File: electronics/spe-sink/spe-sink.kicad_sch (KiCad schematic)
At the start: 18 parts, among them Q1 2N7002P, U1 ATL431LIB, U2 MCP65R41T, U3 AP7375-33

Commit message: Continue work on PD function board schematic
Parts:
- added C10, C12, C14, C6, C8: 100n_X7R_1005M, Applidyne_Capacitor:CAPC1005X60N, symbol appli_capacitor:100n_X7R_1005M
- added C11, C13, C9: 10n_X7R_1005M, Applidyne_Capacitor:CAPC1005X60N, symbol appli_capacitor:10n_X7R_1005M
- added C15: 1u_X5R_1005M, Applidyne_Capacitor:CAPC1005X60N, symbol appli_capacitor:1u_X5R_1005M
- added C16, C17: 22p_X7R_1608M, CAPC1608*, symbol appli_capacitor:22p_X7R_1608M
- added C18, C19: 10u_X7R_2012M, CAPC2012*, symbol appli_capacitor:10u_X7R_2012M
- added C20, C21: 100n_X7R_1608M, CAPC1608*, symbol appli_capacitor:100n_X7R_1608M
- added C5: 4n7_X7R_1608M, CAPC1608*, symbol appli_capacitor:4n7_X7R_1608M
- added C7: 470n_X5R_1005M, CAPC1005X60*, symbol appli_capacitor:470n_X5R_1005M
- added IC1: AT24C02C-SSHM, Applidyne_SOIC:SOIC127P600X330-8L2N, symbol appli_memory:AT24C02C-SSHM
- added P1: CONN_01X03, Applidyne_Connector_Wurth:61300311121, symbol appli_connector_wurth:CONN_01X03
- added R10: 1K5_1005M, Applidyne_Resistor:RESC1005X40N, symbol appli_resistor:1K5_1005M
- added R11: 10K0_1608M, Applidyne_Resistor:RESC1608X50N, symbol appli_resistor:10K0_1608M
- added R12: 100K_1608M, Applidyne_Resistor:RESC1608X50N, symbol appli_resistor:100K_1608M
- added SL1: SOLDER-LINK-3, SJ1608-3*, symbol appli_link:SOLDER-LINK-3
- added SL2: SOLDER-LINK-2-TINY, Applidyne_Link:SJ1005-2N, symbol appli_link:SOLDER-LINK-2-TINY
- added TEST2: CLIP_HOOK_BLUE, Applidyne_Test:KEYSTONE_5117, symbol appli_test_points:CLIP_HOOK_BLUE
- added U4: ADIN1110, Applidyne_QFN:QFN50P600X600X100-40T350X350N, symbol appli_special:ADIN1110
- added U5: AP2112K-3.3, Applidyne_SOT:SOT95P280X145-5L30N, symbol appli_regulator:AP2112K-3.3
- added U6: INA180A3, Applidyne_SOT:SOT23-8P65_280X145L45X30N, symbol appli_analog_devices:INA180A3
- added X1: RH100-25.000-13-F-0715, Applidyne_Crystal:OSCCC320X250X60L90X100N, symbol appli_crystal:RH100-25.000-13-F-0715
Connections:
- net GND: now also C10.2, C11.2, C12.2, C13.2, C14.2, C15.2, C16.2, C17.2, C18.2, C19.2, C20.2, C21.2, C5.2, C6.2, C7.2, C8.2, C9.2, IC1.4 (GND), SL1.3, SL2.2, U4.EP (EP(GND)), U5.2 (GND), U6.2 (GND), X1.2, X1.4
- new net: IC1.7 (WP), R12.2, SL2.1
- new net: C14.1, U4.19 (CEXT_2)
- new net: C15.1, U4.20 (CEXT_3)
- new net: C6.1, C7.1, U4.23 (DLDO_1P1), U4.24 (DVDD_1P1)
- new net: R10.2, U4.26 (TEST1)
- new net: C16.1, U4.8 (XTAL_I/CLK_IN), X1.3
- new net: C17.1, U4.9 (XTAL_O), X1.1
- new net: C18.1, R11.1, U5.1 (VIN)
- new net: R11.2, U5.3 (EN)
- new net: TEST2.1 (PAD), U6.1 (Vout)
- new net: P1.1 (P1), SL1.2
- new net: C5.1, SL1.1
- new net +3.3V: C10.1, C11.1, C12.1, C13.1, C19.1, C20.1, C21.1, C8.1, C9.1, IC1.8 (VCC), R10.1, R12.1, U4.16 (AVDD_H), U4.17 (AVDD_H), U4.22 (AVDD_L), U4.35 (VDDIO), U5.5 (VOUT), U6.5 (VCC)
- no-connect marks 0 -> 2
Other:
- note added: "AVDDH Pin 16"
- note added: "AVDDIO Pin 35"
- note added: "AVDDL Pin 22"
- note added: "Consider ideal diode to prevent LDO being backfed from the output capacitor when line goes low?"
- note added: "DS asks for 0.68uF"
- note added: "Intentionally left open-circuit"
- note added: "Internal bandgap bypass caps"
- note added: "TODO: Connect to MicroMod analog IO"
- note added: "TODO: Consider allowing PWR_EN via MicroMod pin?"
- note added: "TODO: Filter circuit"
- note added: "TODO: Screw terminal block?"
- note added: "TODO: Size shunt for 1A peak loads?"
- note added: "Write protected when high"
- note removed: "ADIN1110 SPE PHY+MAC"
- note removed: "Screw terminal"
- moved on the sheet: C1, C2, C3, C4, Q1, R1, R2, R3, R4, R5, R6, R7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

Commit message: Add MAC+PHY, other parts to PD function board sch
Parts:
- removed C1, C20, C21: 100n_X7R_1608M, CAPC1608*, symbol appli_capacitor:100n_X7R_1608M
- removed C10, C12, C14, C6, C8: 100n_X7R_1005M, Applidyne_Capacitor:CAPC1005X60N, symbol appli_capacitor:100n_X7R_1005M
- removed C11, C13, C9: 10n_X7R_1005M, Applidyne_Capacitor:CAPC1005X60N, symbol appli_capacitor:10n_X7R_1005M
- removed C15: 1u_X5R_1005M, Applidyne_Capacitor:CAPC1005X60N, symbol appli_capacitor:1u_X5R_1005M
- removed C16, C17: 22p_X7R_1608M, CAPC1608*, symbol appli_capacitor:22p_X7R_1608M
- removed C18, C19, C4: 10u_X7R_2012M, CAPC2012*, symbol appli_capacitor:10u_X7R_2012M
- removed C2: 330p_X7R_1608M, CAPC1608*, symbol appli_capacitor:330p_X7R_1608M
- removed C3: 56n_X7R_1608M, CAPC1608*, symbol appli_capacitor:56n_X7R_1608M
- removed C7: 470n_X5R_1005M, CAPC1005X60*, symbol appli_capacitor:470n_X5R_1005M
- removed IC1: AT24C02C-SSHM, Applidyne_SOIC:SOIC127P600X330-8L2N, symbol appli_memory:AT24C02C-SSHM
- removed Q1: 2N7002P, SOT23, symbol appli_transistor:2N7002P
- removed R1, R12: 100K_1608M, Applidyne_Resistor:RESC1608X50N, symbol appli_resistor:100K_1608M
- removed R10: 1K5_1005M, Applidyne_Resistor:RESC1005X40N, symbol appli_resistor:1K5_1005M
- removed R11, R5: 10K0_1608M, Applidyne_Resistor:RESC1608X50N, symbol appli_resistor:10K0_1608M
- removed R2: 9K09_1608M, Applidyne_Resistor:RESC1608X50N, symbol appli_resistor:9K09_1608M
- removed R3: 20K0_1608M, Applidyne_Resistor:RESC1608X50N, symbol appli_resistor:20K0_1608M
- removed R4: 22R_1608M, Applidyne_Resistor:RESC1608X50N, symbol appli_resistor:22R_1608M
- removed R6, R8: 470K_1608M, Applidyne_Resistor:RESC1608X50N, symbol appli_resistor:470K_1608M
- removed R7: 1M_1608M, Applidyne_Resistor:RESC1608X50N, symbol appli_resistor:1M_1608M
- removed R9: 0R_1005M, Applidyne_Resistor:RESC1005X40N, symbol appli_resistor:0R_1005M
- removed SL2: SOLDER-LINK-2-TINY, Applidyne_Link:SJ1005-2N, symbol appli_link:SOLDER-LINK-2-TINY
- removed TEST1: CLIP_HOOK_ORANGE, Applidyne_Test:KEYSTONE_5003, symbol appli_test_points:CLIP_HOOK_ORANGE
- removed TEST2: CLIP_HOOK_BLUE, Applidyne_Test:KEYSTONE_5117, symbol appli_test_points:CLIP_HOOK_BLUE
- removed U1: ATL431LIB, Applidyne_SOT:SOT95P240X110-3L16N, symbol appli_device:ATL431LI_SOT23
- removed U2: MCP65R41T, Applidyne_SOT:SOT95P240X110-6L16N, symbol appli_linear:MCP65R41T
- removed U3: AP7375-33, Applidyne_SOT:SOT95P240X110-3L16N, symbol appli_regulator:AP7375-33
- removed U4: ADIN1110, Applidyne_QFN:QFN50P600X600X100-40T350X350N, symbol appli_special:ADIN1110
- removed U5: AP2112K-3.3, Applidyne_SOT:SOT95P280X145-5L30N, symbol appli_regulator:AP2112K-3.3
- removed U6: INA180A3, Applidyne_SOT:SOT23-8P65_280X145L45X30N, symbol appli_analog_devices:INA180A3
- removed X1: RH100-25.000-13-F-0715, Applidyne_Crystal:OSCCC320X250X60L90X100N, symbol appli_crystal:RH100-25.000-13-F-0715
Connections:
- no-connect marks 2 -> 0
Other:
- added sheet Ethernet MAC+PHY (ethernet.kicad_sch)
- added sheet MicroMod Function Board (micromod.kicad_sch)
- added sheet PoDL Device Handling (podl-pd.kicad_sch.kicad_sch)
- added sheet Power Regulation (power.kicad_sch)
- note added: "Filter/Coupling Network"
- note removed: "AVDDH Pin 16"
- note removed: "AVDDIO Pin 35"
- note removed: "AVDDL Pin 22"
- note removed: "Alternative: 4.54k 10.0k"
- note removed: "Bulk Regulator"
- note removed: "CYA/TESTPOINT"
- note removed: "Consider ideal diode to prevent LDO being backfed from the output capacitor when line goes low?"
- note removed: "DS asks for 0.68uF"
- note removed: "Intentionally left open-circuit"
- note removed: "Internal bandgap bypass caps"
- note removed: "Optional SCCP circuit would go here!"
- note removed: "PoDL DETECTION CIRCUIT"
- note removed: "TODO: Connect to MicroMod analog IO"
- note removed: "TODO: Consider allowing PWR_EN via MicroMod pin?"
- note removed: "TODO: Filter circuit"
- note removed: "TODO: Size shunt for 1A peak loads?"
- note removed: "The PSE tests the PD with a 9-mA to 16-mA constant current pulse. Need to provide the signature voltage from 4.05 V to 4.55 V. Then PSE will enable full power output."
- note removed: "Use precision resistors"
- note removed: "V_{DIV} = (V_{CC}*R_{A})/(R_{A}+R_{B}) = (4.05V*1M)/(1M+470K) = 4.05V"
- note removed: "V_{HYSTERESIS} = (V_{CC}*R_{A})/(R_{A}+R_{B}) = (3.3V*10K)/(10K+470K) = ~0.067V"
- note removed: "V_{REF}=2500mV I_{REF}=0.4uA V_{OUT} = (1+R_{A}/R_{B})*V_{REF}-I_{REF}*R_{A} = (1+9K09/20K)*2.5V (I_{REF} basically 0) = 3.656V"
- note removed: "Write protected when high"

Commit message: Building out PDoE filter/isolation, etc
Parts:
- added D4: CD-HD2006L, Applidyne_Device:CD-HD2x(L), symbol appli_device:CD-HD2006L
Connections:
- net GND: now also D4.4 (-)
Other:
- sheet Ethernet MAC+PHY ports: added none; removed RXN, RXP, TXN, TXP
- note removed: "Rectifier"
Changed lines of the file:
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@@
+    (stroke (width 0) (type default))
+  )
+  (wire (pts (xy 86.36 123.19) (xy 104.14 123.19))
     (stroke (width 0) (type default))
   )
@@
     (stroke (width 0) (type default))
   )
+  (wire (pts (xy 86.36 101.6) (xy 86.36 123.19))
+    (stroke (width 0) (type default))
+  )
   (wire (pts (xy 165.1 50.8) (xy 203.2 50.8))
     (stroke (width 0) (type default))
   )
+  (wire (pts (xy 92.71 101.6) (xy 92.71 102.87))
+    (stroke (width 0) (type default))
+  )
   (wire (pts (xy 35.56 60.96) (xy 35.56 64.77))
     (stroke (width 0) (type default))
@@
     (stroke (width 0) (type default))
   )
+  (wire (pts (xy 96.52 113.03) (xy 93.98 113.03))
+    (stroke (width 0) (type default))
+  )
   (wire (pts (xy 43.18 48.26) (xy 54.61 48.26))
     (stroke (width 0) (type default))
   )
+  (wire (pts (xy 104.14 120.65) (xy 104.14 123.19))
+    (stroke (width 0) (type default))
+  )
   (wire (pts (xy 43.18 50.8) (xy 54.61 50.8))
     (stroke (width 0) (type default))
   )
+  (wire (pts (xy 104.14 105.41) (xy 104.14 102.87))
+    (stroke (width 0) (type default))
+  )
+  (wire (pts (xy 111.76 113.03) (xy 119.38 113.03))
+    (stroke (width 0) (type default))
+  )
   (wire (pts (xy 35.56 69.85) (xy 35.56 72.39))
     (stroke (width 0) (type default))
   )
+  (wire (pts (xy 92.71 102.87) (xy 104.14 102.87))
+    (stroke (width 0) (type default))
+  )
   (wire (pts (xy 50.8 60.96) (xy 54.61 60.96))
     (stroke (width 0) (type default))
   )
+  (wire (pts (xy 93.98 113.03) (xy 93.98 114.3))
+    (stroke (width 0) (type default))
+  )
   (wire (pts (xy 40.64 60.96) (xy 35.56 60.96))
     (stroke (width 0) (type default))
-  )
-  (text "Rectifier" (at 92.71 110.49 0)
-    (effects (font (size 1.27 1.27)) (justify left bottom))
   )
   (text "Filter/Coupling Network" (at 82.55 77.47 0)
@@
   (text "Spec asks for <400nF input capacitance" (at 38.1 31.75 0)
     (effects (font (size 1.27 1.27)) (justify left bottom))
+  )
+  (symbol (lib_id "appli_device:CD-HD2006L") (at 104.14 113.03 0) (unit 1)
+    (in_bom yes) (on_board yes) (dnp no)
+    (property "Reference" "D4" (at 109.22 102.87 0)
+      (effects (font (size 1.27 1.27)))
+    )
+    (property "Value" "CD-HD2006L" (at 114.3 105.41 0)
+      (effects (font (size 1.27 1.27)))
+    )
+    (property "Footprint" "Applidyne_Device:CD-HD2x(L)" (at 110.236 118.999 0)
+      (effects (font (size 0.508 0.508)) (justify left bottom) hide)
+    )
+    (property "Datasheet" "https://www.bourns.com/docs/Product-Datasheets/cd-hd2xl.pdf" (at 110.236 119.634 0)
+      (effects (font (size 0.508 0.508)) (justify left bottom) hide)
+    )
+    (property "manf" "Bourns Inc" (at 110.236 120.904 0)
+      (effects (font (size 0.508 0.508)) (justify left bottom) hide)
+    )
+    (property "manf#" "CD-HD2006L" (at 110.236 121.539 0)
+      (effects (font (size 0.508 0.508)) (justify left bottom) hide)
+    )
+    (property "Supplier" "Digikey" (at 110.236 122.174 0)
+      (effects (font (size 0.508 0.508)) (justify left bottom) hide)
+    )
+    (property "Supplier Part No" "118-CD-HD2006LCT-ND" (at 110.236 122.809 0)
+      (effects (font (size 0.508 0.508)) (justify left bottom) hide)
+    )
+    (property "Supplier URL" "https://www.digikey.com.au/en/products/detail/bourns-inc/CD-HD2006L/6571504" (at 110.236 123.444 0)
+      (effects (font (size 0.508 0.508)) (justify left bottom) hide)
+    )
+    (property "Supplier Price" "1.10" (at 110.236 124.079 0)
+      (effects (font (size 0.508 0.508)) (justify left bottom) hide)
+    )
+    (property "Supplier Price Break" "10" (at 110.236 124.714 0)
+      (effects (font (size 0.508 0.508)) (justify left bottom) hide)
+    )
+    (pin "1")
+    (pin "2")
+    (pin "3")
+    (pin "4")
+    (instances
+      (project "spe-sink"
+        (path "/f0a501c7-1ad1-4c59-9255-3d6aa4545d8b"
+          (reference "D4") (unit 1)
+        )
+      )
+    )
   )
   (symbol (lib_id "appli_connector_wurth:CONN_01X03") (at 38.1 50.8 180) (unit 1)
@@
         (path "/f0a501c7-1ad1-4c59-9255-3d6aa4545d8b"
           (reference "#PWR09") (unit 1)
+        )
+      )
+    )
+  )
+  (symbol (lib_id "appli_power:GND") (at 93.98 114.3 0) (unit 1)
+    (in_bom yes) (on_board yes) (dnp no) (fields_autoplaced)
+    (property "Reference" "#PWR049" (at 93.98 120.65 0)
+      (effects (font (size 1.27 1.27)) hide)
+    )
+    (property "Value" "GND" (at 93.98 119.38 0)
+      (effects (font (size 1.27 1.27)))
+    )
+    (property "Footprint" "" (at 93.98 114.3 0)
+      (effects (font (size 1.27 1.27)) hide)
+    )
+    (property "Datasheet" "" (at 93.98 114.3 0)
+      (effects (font (size 1.27 1.27)) hide)
+    )
+    (pin "1")
+    (instances
+      (project "spe-sink"
+        (path "/f0a501c7-1ad1-4c59-9255-3d6aa4545d8b"
+          (reference "#PWR049") (unit 1)
         )
       )
@@
       (effects (font (size 1.27 1.27)) (justify left top))
     )
-    (pin "TXN" input (at 127 43.18 180)
-      (effects (font (size 1.27 1.27)) (justify left))
-    )
-    (pin "TXP" input (at 127 45.72 180)
-      (effects (font (size 1.27 1.27)) (justify left))
-    )
-    (pin "RXP" input (at 127 48.26 180)
-      (effects (font (size 1.27 1.27)) (justify left))
-    )
     (pin "{SPI}" bidirectional (at 165.1 43.18 0)
       (effects (font (size 1.27 1.27)) (justify right))
@@
       (effects (font (size 1.27 1.27)) (justify right))
     )
-    (pin "RXN" input (at 127 50.8 180)
-      (effects (font (size 1.27 1.27)) (justify left))
-    )
-    (instances
+    (instances

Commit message: PD function board schematic progress
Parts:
- added C22 (x2): 220n_X7R_1005M, Applidyne_Capacitor:CAPC1005X60N, symbol appli_capacitor:220n_X7R_1005M
- added C23: 100n_X7R_1608M, Applidyne_Capacitor:CAPC1608X90N, symbol appli_capacitor:100n_X7R_1608M
- added C25, C26, C27: 470n_X7R_2012M_100V, Applidyne_Capacitor:CAPC2012X110N, symbol appli_capacitor:470n_X7R_2012M_100V
- added C29: 1n_X7R_3216M_2kV, Applidyne_Capacitor:CAPC3216X135N, symbol appli_capacitor:1n_X7R_3216M_2kV
- added L1: WE-STST_74930000, Applidyne_Inductor:WE-STST, symbol appli_inductor:WE-STST_74930000
- added L2: COUPLED_47uH_1500mA_340mOhm, Applidyne_Inductor:WE-MCRI-1040, symbol appli_inductor:COUPLED_47uH_1500mA_340mOhm
- added L3: COMM_MODE_1000uH_800mA_0.3R, Applidyne_Inductor:WE-SL2, symbol appli_inductor:COMM_MODE_1000uH_800mA_0.2R
- added R26: 100R_1608M, Applidyne_Resistor:RESC1608X50N, symbol appli_resistor:100R_1608M
- C5: footprint CAPC1608* -> Applidyne_Capacitor:CAPC1608X90N
- SL1: footprint SJ1608-3* -> Applidyne_Link:SJ1608-3N
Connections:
- net GND: now also C23.2, C29.2
- net PoDL Device Handling/PoDL+: now reaches D4.1 (+)
- net at D4.2 (∿): now also L2.4
- net at D4.3 (∿): now also L2.1
- net at P1.2 (P2): now also L3.2
- net at P1.3 (P3): now also L3.1
- new net: C27.1, L2.2, L3.3
- new net: C26.1, L2.3, L3.4
- new net: C27.2, L1.7
- new net: C22.1, L1.1
- new net: C22.1, L1.2
- new net: C25.2, L1.3, R26.1
- new net: C25.1, L1.4
- new net: C23.1, L1.5
- new net: C26.2, L1.6
- new net: C29.1, R26.2
- new net Ethernet MAC+PHY/DATA+: C22.2
- new net Ethernet MAC+PHY/DATA-: C22.2
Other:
- sheet Ethernet MAC+PHY ports: added DATA+, DATA-; removed none
- sheet PoDL Device Handling ports: added PoDL+; removed none
- sheet Power Regulation ports: added PoDL+; removed none
- note added: "BRIDGE/LOAD 0R IF TRANSFORMER CENTER TAP CAPACITOR USED"
- note added: "Common Mode Choke"
- note added: "Differential Mode Inductor"
- note added: "ESD Protection"
- note added: "Isolation Transformer"
- note added: "Rectification"
- note added: "SPE UTP"
- note removed: "Filter/Coupling Network"
- note removed: "Input filter"
- note removed: "Spec asks for <400nF input capacitance"
- note removed: "TODO: Screw terminal block?"
- moved on the sheet: C5, D4, P1, SL1

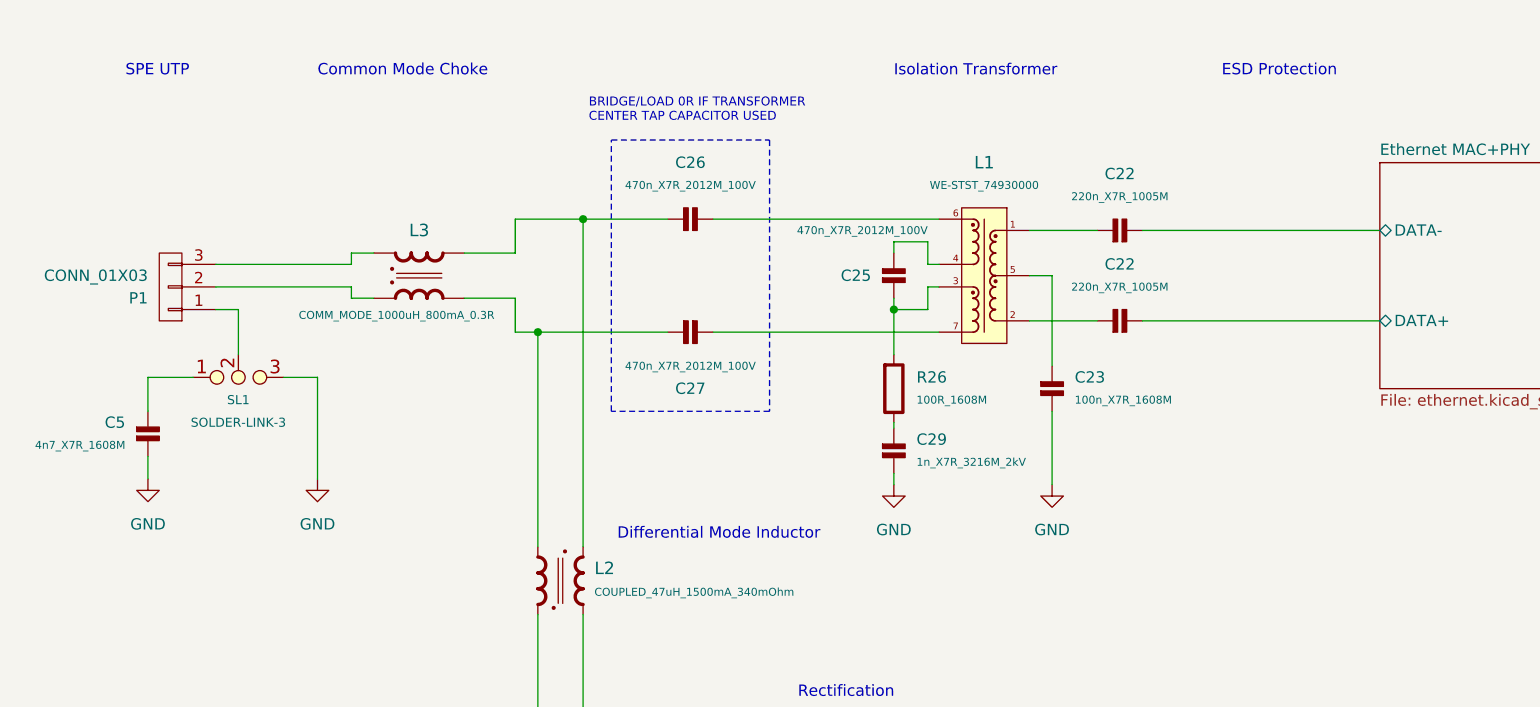
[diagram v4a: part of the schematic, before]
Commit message: PD function board bulk regulator, cleanup, part placement
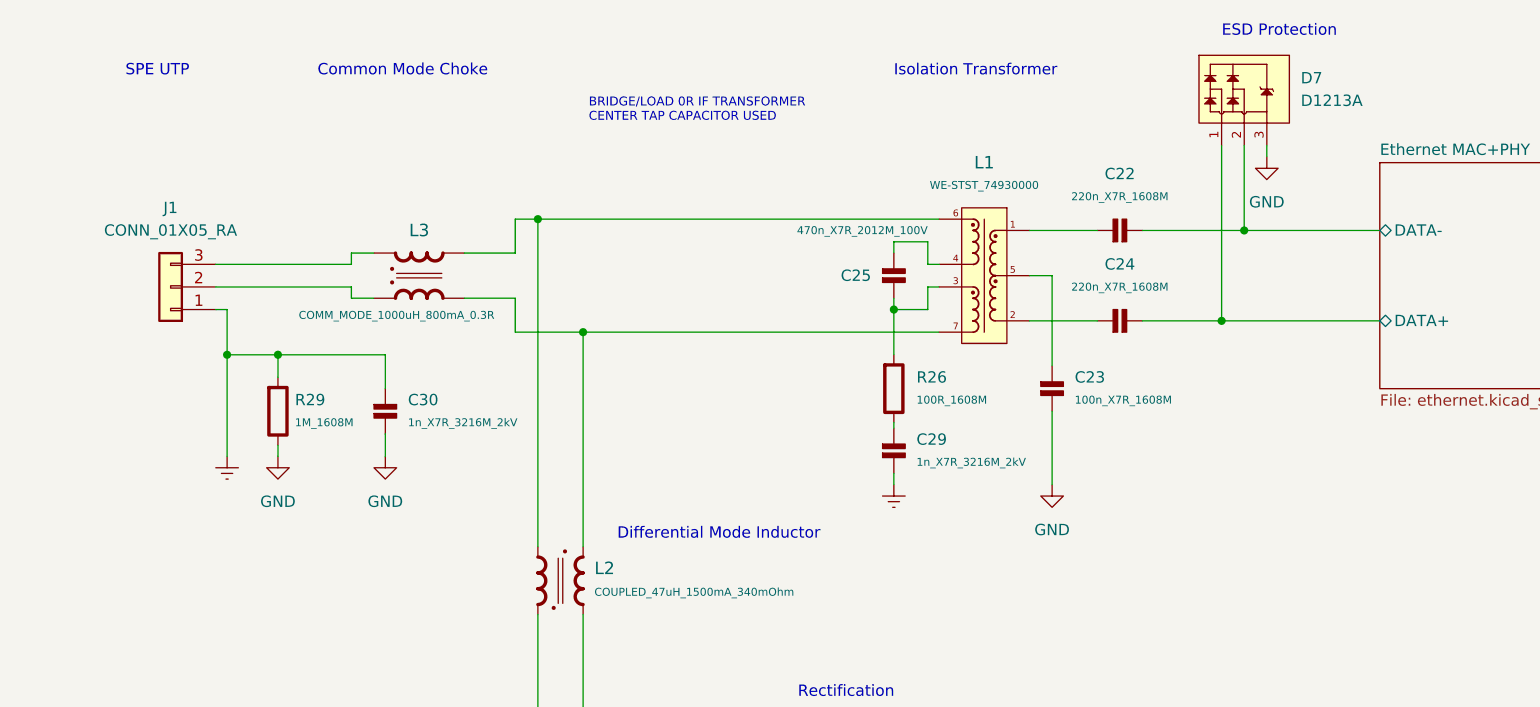
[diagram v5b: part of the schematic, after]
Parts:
- removed C22 (x2): 220n_X7R_1005M, Applidyne_Capacitor:CAPC1005X60N, symbol appli_capacitor:220n_X7R_1005M
- removed C26, C27: 470n_X7R_2012M_100V, Applidyne_Capacitor:CAPC2012X110N, symbol appli_capacitor:470n_X7R_2012M_100V
- removed C5: 4n7_X7R_1608M, Applidyne_Capacitor:CAPC1608X90N, symbol appli_capacitor:4n7_X7R_1608M
- removed P1: CONN_01X03, Applidyne_Connector_Wurth:61300311121, symbol appli_connector_wurth:CONN_01X03
- removed SL1: SOLDER-LINK-3, Applidyne_Link:SJ1608-3N, symbol appli_link:SOLDER-LINK-3
- added C22, C24: 220n_X7R_1608M, Applidyne_Capacitor:CAPC1608X90N, symbol appli_capacitor:220n_X7R_1608M
- added C30: 1n_X7R_3216M_2kV, Applidyne_Capacitor:CAPC3216X135N, symbol appli_capacitor:1n_X7R_3216M_2kV
- added D7: D1213A, Applidyne_SOT:SOT95P240X110-3L16N, symbol appli_device:D1213A
- added J1: CONN_01X05_RA, Applidyne_Connector:CUI_TBL009-254-03, symbol appli_connector:CONN_01X03_RA
- added R29: 1M_1608M, Applidyne_Resistor:RESC1608X50N, symbol appli_resistor:1M_1608M
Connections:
- net Ethernet MAC+PHY/DATA+: now also C24.2, D7.1 (A1)
- net Ethernet MAC+PHY/DATA-: now also C22.2, D7.2 (C2)
- net GND: now also C30.2, D7.3, R29.2; no longer C29.2
- net at L3.1: now also J1.3 (Pin_3)
- net at L3.2: now also J1.2 (Pin_2)
- net at L3.3: now also L1.7, L2.3; no longer L2.2
- net at L3.4: now also L1.6, L2.2; no longer L2.3
- net at L1.1: now also C22.1
- net at L1.2: now also C24.1
- new net Earth: C29.2, C30.1, J1.1 (Pin_1), R29.1

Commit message: PD sink board routing, minor sch changes, etc
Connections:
- net at L1.7, L2.3, L3.3: now also L1.6, L2.2, L3.4
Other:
- note removed: "BRIDGE/LOAD 0R IF TRANSFORMER CENTER TAP CAPACITOR USED"
- moved on the sheet: L2
